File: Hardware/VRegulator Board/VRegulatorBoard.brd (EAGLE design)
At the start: 20.3 x 18.7 mm, 10 parts

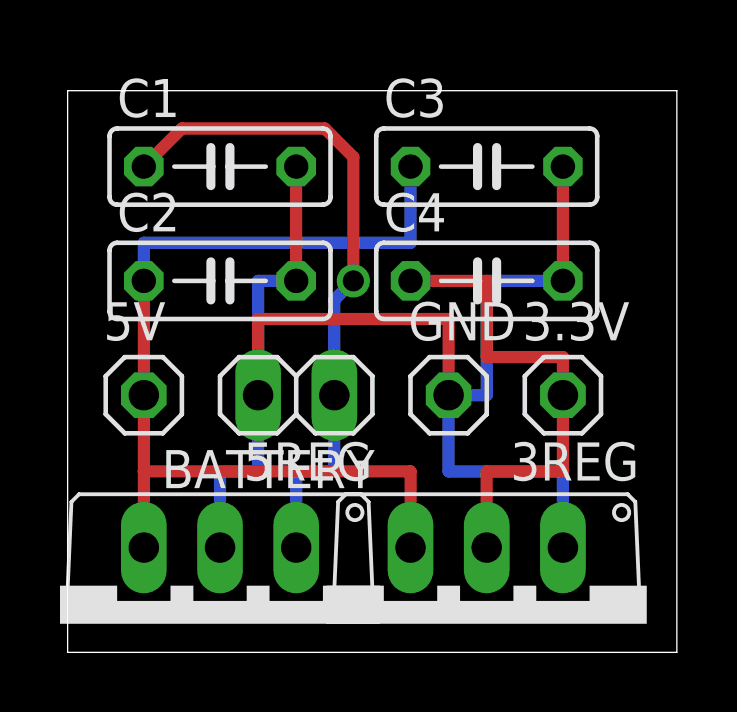
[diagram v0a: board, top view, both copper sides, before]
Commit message: added indesign file
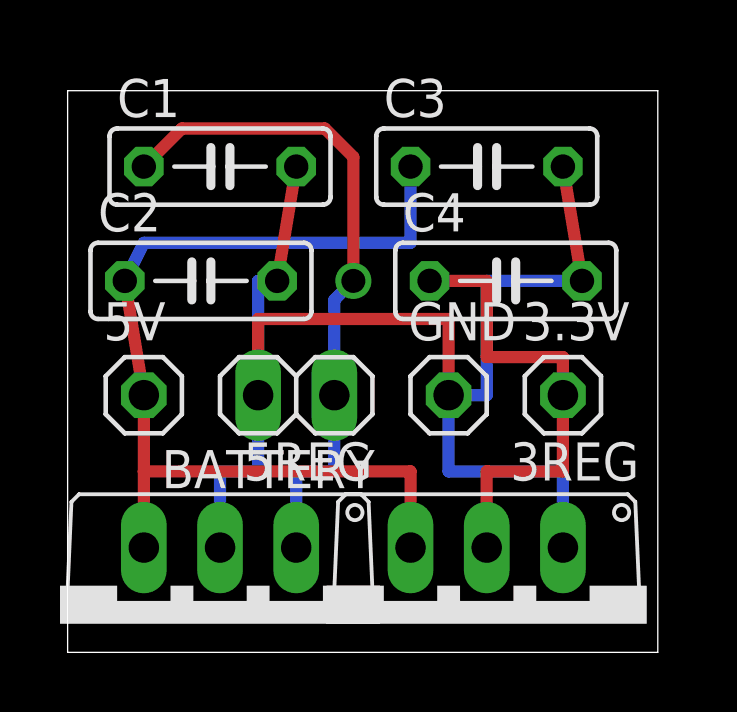
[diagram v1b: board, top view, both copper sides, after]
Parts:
- moved C2 0.63 mm to (4.45, 73.7)
- moved C4 0.63 mm to (14.6, 73.7)
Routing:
- net N$4: track 16.5 -> 15.9 mm
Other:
- board size 20.3 x 18.7 mm -> 19.7 x 18.7 mm
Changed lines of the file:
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@@
 <board>
 <plain>
-<wire x1="0" y1="61.2775" x2="20.3075" y2="61.2775" width="0" layer="20"/>
-<wire x1="20.3075" y1="61.2775" x2="20.3075" y2="80" width="0" layer="20"/>
-<wire x1="20.3075" y1="80" x2="0" y2="80" width="0" layer="20"/>
+<wire x1="0" y1="61.2775" x2="19.6725" y2="61.2775" width="0" layer="20"/>
+<wire x1="19.6725" y1="61.2775" x2="19.6725" y2="80" width="0" layer="20"/>
+<wire x1="19.6725" y1="80" x2="0" y2="80" width="0" layer="20"/>
 <wire x1="0" y1="80" x2="0" y2="61.2775" width="0" layer="20"/>
 </plain>
@@
 <element name="BATTERY" library="pinhead" package="1X02" value="" x="7.62" y="69.85" rot="R180"/>
 <element name="C1" library="adafruit" package="C050-025X075" value="" x="5.08" y="77.47"/>
-<element name="C2" library="adafruit" package="C050-025X075" value="" x="5.08" y="73.66"/>
+<element name="C2" library="adafruit" package="C050-025X075" value="" x="4.445" y="73.66"/>
 <element name="C3" library="adafruit" package="C050-025X075" value="" x="13.97" y="77.47"/>
-<element name="C4" library="adafruit" package="C050-025X075" value="" x="13.97" y="73.66"/>
+<element name="C4" library="adafruit" package="C050-025X075" value="" x="14.605" y="73.66"/>
 <element name="GND" library="pinhead" package="1X01" value="" x="12.7" y="69.85"/>
 <element name="5REG" library="linear" package="TO220V" value="7805TV" x="5.08" y="62.23" rot="R180"/>
@@
 <wire x1="8.5725" y1="78.74" x2="3.81" y2="78.74" width="0.4064" layer="1"/>
 <wire x1="3.81" y1="78.74" x2="2.54" y2="77.47" width="0.4064" layer="1"/>
-<via x="9.525" y="73.66" extent="1-16" drill="0.7" shape="square"/>
+<via x="9.525" y="73.66" extent="1-16" drill="0.8" shape="square"/>
 </signal>
 <signal name="N$2">
@@
 <contactref element="C3" pad="1"/>
 <contactref element="5V" pad="1"/>
-<wire x1="2.54" y1="73.66" x2="2.54" y2="69.85" width="0.4064" layer="1"/>
+<wire x1="1.905" y1="73.66" x2="2.54" y2="69.85" width="0.4064" layer="1"/>
 <wire x1="2.54" y1="69.85" x2="2.54" y2="67.31" width="0.4064" layer="1"/>
 <contactref element="3REG" pad="3"/>
@@
 <wire x1="2.54" y1="67.31" x2="11.43" y2="67.31" width="0.4064" layer="1"/>
 <wire x1="11.43" y1="67.31" x2="11.43" y2="64.77" width="0.4064" layer="1"/>
-<wire x1="2.54" y1="73.66" x2="2.54" y2="74.93" width="0.4064" layer="16"/>
+<wire x1="1.905" y1="73.66" x2="2.54" y2="74.93" width="0.4064" layer="16"/>
 <wire x1="2.54" y1="74.93" x2="11.43" y2="74.93" width="0.4064" layer="16"/>
 <wire x1="11.43" y1="74.93" x2="11.43" y2="77.47" width="0.4064" layer="16"/>
@@
 <wire x1="16.51" y1="67.31" x2="13.97" y2="67.31" width="0.4064" layer="1"/>
 <wire x1="13.97" y1="67.31" x2="13.97" y2="64.77" width="0.4064" layer="1"/>
-<wire x1="11.43" y1="73.66" x2="13.97" y2="73.66" width="0.4064" layer="1"/>
+<wire x1="12.065" y1="73.66" x2="13.97" y2="73.66" width="0.4064" layer="1"/>
 <wire x1="13.97" y1="73.66" x2="13.97" y2="71.12" width="0.4064" layer="1"/>
 <wire x1="13.97" y1="71.12" x2="16.51" y2="71.12" width="0.4064" layer="1"/>
@@
 <contactref element="C3" pad="2"/>
 <contactref element="C4" pad="2"/>
-<wire x1="7.62" y1="77.47" x2="7.62" y2="73.66" width="0.4064" layer="1"/>
-<wire x1="16.51" y1="73.66" x2="13.97" y2="73.66" width="0.4064" layer="16"/>
+<wire x1="7.62" y1="77.47" x2="6.985" y2="73.66" width="0.4064" layer="1"/>
+<wire x1="17.145" y1="73.66" x2="13.97" y2="73.66" width="0.4064" layer="16"/>
 <wire x1="13.97" y1="73.66" x2="13.97" y2="69.85" width="0.4064" layer="16"/>
 <wire x1="13.97" y1="69.85" x2="12.7" y2="69.85" width="0.4064" layer="16"/>
@@
 <wire x1="16.51" y1="67.31" x2="16.51" y2="64.77" width="0.4064" layer="16"/>
 <wire x1="6.35" y1="69.85" x2="6.35" y2="73.66" width="0.4064" layer="16"/>
-<wire x1="6.35" y1="73.66" x2="7.62" y2="73.66" width="0.4064" layer="16"/>
+<wire x1="6.35" y1="73.66" x2="6.985" y2="73.66" width="0.4064" layer="16"/>
 <wire x1="6.35" y1="69.85" x2="6.35" y2="67.31" width="0.4064" layer="16"/>
 <wire x1="6.35" y1="67.31" x2="5.08" y2="67.31" width="0.4064" layer="16"/>
 <wire x1="5.08" y1="67.31" x2="5.08" y2="64.77" width="0.4064" layer="16"/>
-<wire x1="16.51" y1="77.47" x2="16.51" y2="73.66" width="0.4064" layer="1"/>
+<wire x1="16.51" y1="77.47" x2="17.145" y2="73.66" width="0.4064" layer="1"/>
 <wire x1="12.7" y1="69.85" x2="12.7" y2="72.39" width="0.4064" layer="1"/>
 <wire x1="12.7" y1="72.39" x2="6.35" y2="72.39" width="0.4064" layer="1"/>
